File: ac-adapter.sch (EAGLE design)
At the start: 55 parts, among them IC1 STR-Y6735, IC2 TL431, Q1 TLP621-1, T1 COMMON_FILTER-SU10VFC, T2 TRANSFORMAER_FLYBACK-PQ2620

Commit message: 微修正
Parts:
- added HT1: HEATSINK-2, my_connector:HEATSINK-2
- D5, D6: value 0.1A -> 1N4148; device my_rcl:DIODE-2 -> my_rcl:DIODE-1N4148W
- R3: device my_rcl:R-2.5 -> my_rcl:R-1608
- R7, R8: device my_rcl:R-2.5 -> my_rcl:R-2012
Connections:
- net PGND: now also HT1.HT
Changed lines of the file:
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@@
 <layer number="115" name="sd" color="13" fill="1" visible="yes" active="yes"/>
 <layer number="116" name="Patch_BOT" color="7" fill="1" visible="yes" active="yes"/>
+<layer number="117" name="BACKMAAT1" color="7" fill="1" visible="no" active="no"/>
 <layer number="118" name="Rect_Pads" color="7" fill="1" visible="no" active="no"/>
+<layer number="119" name="KAP_TEKEN" color="7" fill="1" visible="no" active="no"/>
+<layer number="120" name="KAP_MAAT1" color="7" fill="1" visible="no" active="no"/>
 <layer number="121" name="_tsilk" color="7" fill="1" visible="yes" active="yes"/>
 <layer number="122" name="_bsilk" color="7" fill="1" visible="yes" active="yes"/>
@@
 <layer number="128" name="_bValues" color="7" fill="1" visible="yes" active="yes"/>
 <layer number="129" name="Mask" color="7" fill="1" visible="no" active="no"/>
+<layer number="130" name="SMDSTROOK" color="7" fill="1" visible="no" active="no"/>
 <layer number="131" name="tAdjust" color="7" fill="1" visible="yes" active="yes"/>
 <layer number="132" name="bAdjust" color="7" fill="1" visible="yes" active="yes"/>
+<layer number="133" name="bottom_silk" color="7" fill="1" visible="no" active="no"/>
 <layer number="144" name="Drill_legend" color="7" fill="1" visible="yes" active="yes"/>
 <layer number="150" name="Notes" color="7" fill="1" visible="yes" active="yes"/>
@@
 <layer number="230" name="230bmp" color="7" fill="1" visible="no" active="no"/>
 <layer number="231" name="231bmp" color="7" fill="1" visible="no" active="no"/>
+<layer number="232" name="Eagle3D_PG2" color="7" fill="1" visible="no" active="no"/>
+<layer number="233" name="Eagle3D_PG3" color="7" fill="1" visible="no" active="no"/>
 <layer number="248" name="Housing" color="7" fill="1" visible="yes" active="yes"/>
 <layer number="249" name="Edge" color="7" fill="1" visible="yes" active="yes"/>
@@
 <part name="C4" library="my_rcl" deviceset="C" device="-5" value="1000pF1kV"/>
 <part name="R1" library="my_rcl" deviceset="R" device="-10" value="0.47"/>
-<part name="D5" library="my_rcl" deviceset="DIODE" device="-2" value="0.1A"/>
+<part name="D5" library="my_rcl" deviceset="DIODE" device="-1N4148W" value="1N4148"/>
 <part name="R2" library="my_rcl" deviceset="R" device="-7.5" value="10"/>
-<part name="D6" library="my_rcl" deviceset="DIODE" device="-2" value="0.1A"/>
-<part name="R3" library="my_rcl" deviceset="R" device="-2.5" value="6.8k"/>
+<part name="D6" library="my_rcl" deviceset="DIODE" device="-1N4148W" value="1N4148"/>
+<part name="R3" library="my_rcl" deviceset="R" device="-1608" value="6.8k"/>
 <part name="R4" library="my_rcl" deviceset="R" device="-1608" value="DNP"/>
 <part name="C5" library="my_rcl" deviceset="CPOL" device="E2.5-8" value="100uF35V"/>
@@
 <part name="D8" library="my_rcl" deviceset="DIODE2" device="" value="60V10A"/>
 <part name="C10" library="my_rcl" deviceset="C" device="-1608" value="1000p"/>
-<part name="R7" library="my_rcl" deviceset="R" device="-2.5" value="22"/>
-<part name="R8" library="my_rcl" deviceset="R" device="-2.5" value="22"/>
+<part name="R7" library="my_rcl" deviceset="R" device="-2012" value="22"/>
+<part name="R8" library="my_rcl" deviceset="R" device="-2012" value="22"/>
 <part name="C11" library="my_rcl" deviceset="C" device="-1608" value="1000p"/>
 <part name="C12" library="my_rcl" deviceset="CPOL" device="E5-13" value="1000uF35V"/>
@@
 <part name="SJ1" library="Connector_Robotech" deviceset="SJ" device="1608" value="F2"/>
 <part name="SJ2" library="Connector_Robotech" deviceset="SJ" device="1608" value="F1"/>
+<part name="HT1" library="my_connector" deviceset="HEATSINK" device="-2" value="HEATSINK-2"/>
 </parts>
 <sheets>
@@
 <attribute name="NAME" x="215.9" y="27.94" size="1.778" layer="95" rot="R90"/>
 <attribute name="VALUE" x="222.25" y="27.94" size="1.778" layer="96" rot="R90"/>
+</instance>
+<instance part="HT1" gate="G$2" x="60.96" y="2.54" smashed="yes">
+<attribute name="NAME" x="60.96" y="3.81" size="2.54" layer="95"/>
+<attribute name="VALUE" x="60.96" y="-1.27" size="2.54" layer="96"/>
 </instance>
 </instances>
@@
 <wire x1="142.24" y1="33.02" x2="147.32" y2="33.02" width="0.1524" layer="91"/>
 <junction x="147.32" y="33.02"/>
-</segment>
-</net>
+<pinref part="HT1" gate="G$2" pin="HT"/>
+<wire x1="71.12" y1="-5.08" x2="60.96" y2="-5.08" width="0.1524" layer="91"/>
+<wire x1="60.96" y1="-5.08" x2="60.96" y2="-2.54" width="0.1524" layer="91"/>
+<junction x="71.12" y="-5.08"/>
+</segment>
+</net>

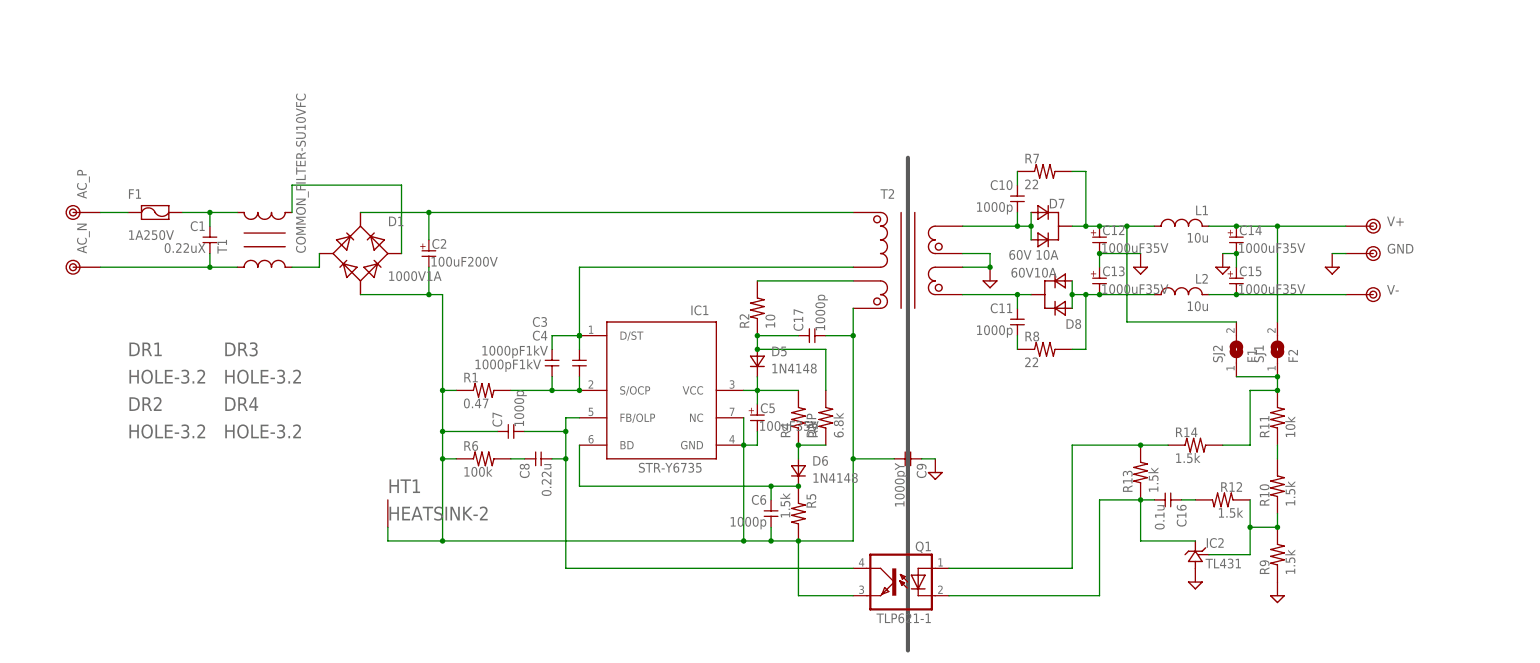
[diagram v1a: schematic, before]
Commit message: BM1Q011FJを使う
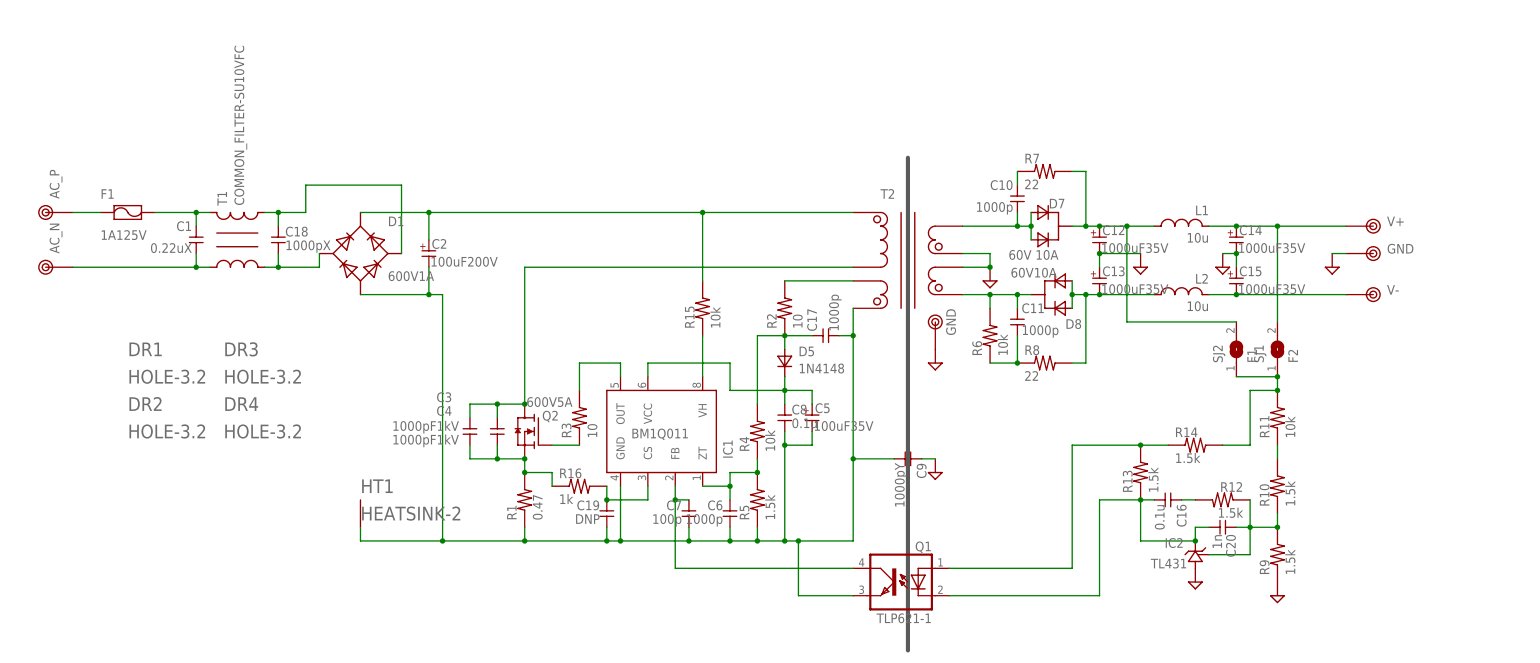
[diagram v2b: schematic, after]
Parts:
- removed D6: 1N4148, my_rcl:DIODE-1N4148W
- added C18: 1000pX, my_rcl:C-5
- added C19: DNP, my_rcl:C-1608
- added C20: 1n, my_rcl:C-1608
- added Q2: 600V5A, my_ic:NMOS
- added R15: 10k, my_rcl:R-2012
- added R16: 1k, my_rcl:R-1608
- added TP6: GND, my_connector:TESTPIN-BIG
- C2: device my_rcl:CPOLE5-10.5A2 -> my_rcl:CPOLE7.5-16A2
- C7: value 1000p -> 100p
- C8: value 0.22u -> 0.1u; device my_rcl:C-1608 -> my_rcl:C-2012
- D1: value 1000V1A -> 600V1A
- F1: value 1A250V -> 1A125V
- IC1: value STR-Y6735 -> BM1Q011; device my_ic:STR-Y6700 -> my_ic:BM1Q011
- R2: device my_rcl:R-7.5 -> my_rcl:R-2012
- R3: value 6.8k -> 10; device my_rcl:R-1608 -> my_rcl:R-2012
- R4: value DNP -> 10k
- R6: value 100k -> 10k; device my_rcl:R-2.5 -> my_rcl:R-1608
- T2: value TRANSFORMAER_FLYBACK-PQ2620 -> TRANSFORMAER_FLYBACK-PQ2620-2; device my_rcl:TRANSFORMAER_FLYBACK-PQ2620 -> my_rcl:TRANSFORMAER_FLYBACK-PQ2620-2
- TP1, TP2, TP3, TP4, TP5: device my_connector:TESTPIN-BIG -> my_connector:TESTPIN-LARGE
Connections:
- new net N$12: C3.2, C4.2, Q2.S, R1.2, R16.1
- new net N$19: C7.1, IC1.FB, Q1.COL
- net GND: now also TP6.1
- net N$11: now also R4.2; no longer R3.2
- net N$13: now also IC1.OUT, R3.2; no longer C6.1, D6.K, IC1.BD, R5.1
- net N$14: now also Q2.G; no longer D6.A, R4.1
- net N$15: now also C19.1, IC1.CS, R16.2; no longer C7.2, C8.2, IC1.FB/OLP, Q1.COL
- net N$16: now also C18.1, D1.AC2, T1.3; no longer C8.1, R6.2
- net N$18: now also R6.2
- net N$22: now also R6.1
- net N$26: now also C20.1
- net N$28: now also C20.2
- net N$4: now also C18.2
- net N$5: now also IC1.VH, R15.1; no longer D1.AC2, T1.3
- net N$7: now also C6.1, IC1.ZT, R4.1, R5.2; no longer C3.2, C4.2, IC1.S/OCP, R1.2
- net PGND: now also C19.2, C7.2, C8.2, R5.1; no longer C7.1, IC1.NC, R5.2, R6.1
- net SW: now also Q2.D; no longer IC1.D/ST
- net VCC: now also C8.1; no longer R4.2
- net VP: now also R15.2
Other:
- moved on the sheet: C1, C17, C3, C4, C5, C6, C7, C8, D5, F1, HT1, IC1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

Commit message: PGND変更
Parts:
- added FB1: FB, my_rcl:FB
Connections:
- new net N$20: FB1.1, HT1.HT
- net PGND: now also FB1.2; no longer HT1.HT
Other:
- moved on the sheet: HT1

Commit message: tiny
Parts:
- added D2: GREEN, my_rcl:LED-SMD1608
- added R17, R18: 10k, my_rcl:R-1608
- added V1: Varistor, my_rcl:C-5
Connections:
- new net N$21: D2.K, R17.2
- net GND: now also R17.1
- net N$14: now also R18.1
- net N$2: now also V1.2
- net N$3: now also V1.1
- net N$9: now also D2.A
- net PGND: now also R18.2
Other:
- moved on the sheet: C1, C18, C2, C3, C4, D1, F1, FB1, HT1, Q2, R1, R16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

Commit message: GaN
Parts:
- removed FB1: FB, my_rcl:FB
- removed HT1: HEATSINK-2, my_connector:HEATSINK-2
- removed Q2: 600V5A, my_ic:NMOS
- removed R18: 10k, my_rcl:R-1608
- added C21: (no value), my_rcl:C-1608
- added D3: (no value), my_rcl:ZENER-SMD
- added IC3: NV6113, my_ic:NV6113
- R3: value 10 -> (none); device my_rcl:R-2012 -> my_rcl:R-1608
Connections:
- new net N$24: D3.C, IC3.DZ
- net N$12: now also C21.2, D3.A, IC3.S; no longer Q2.S
- net N$13: now also IC3.PWM; no longer R3.2
- net N$14: now also C21.1; no longer Q2.G, R18.1
- net N$20: now also IC3.VDD, R3.2; no longer FB1.1, HT1.HT
- net PGND: no longer FB1.2, R18.2
- net SW: now also IC3.D; no longer Q2.D
- net VCC: now also IC3.VCC
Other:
- moved on the sheet: C10, C11, C12, C13, C14, C15, C16, C17, C19, C20, C3, C4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
